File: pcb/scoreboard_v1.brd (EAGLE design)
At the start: 150 x 90 mm, 28 parts, among them U1 ESP-12F, U2 AP2111H

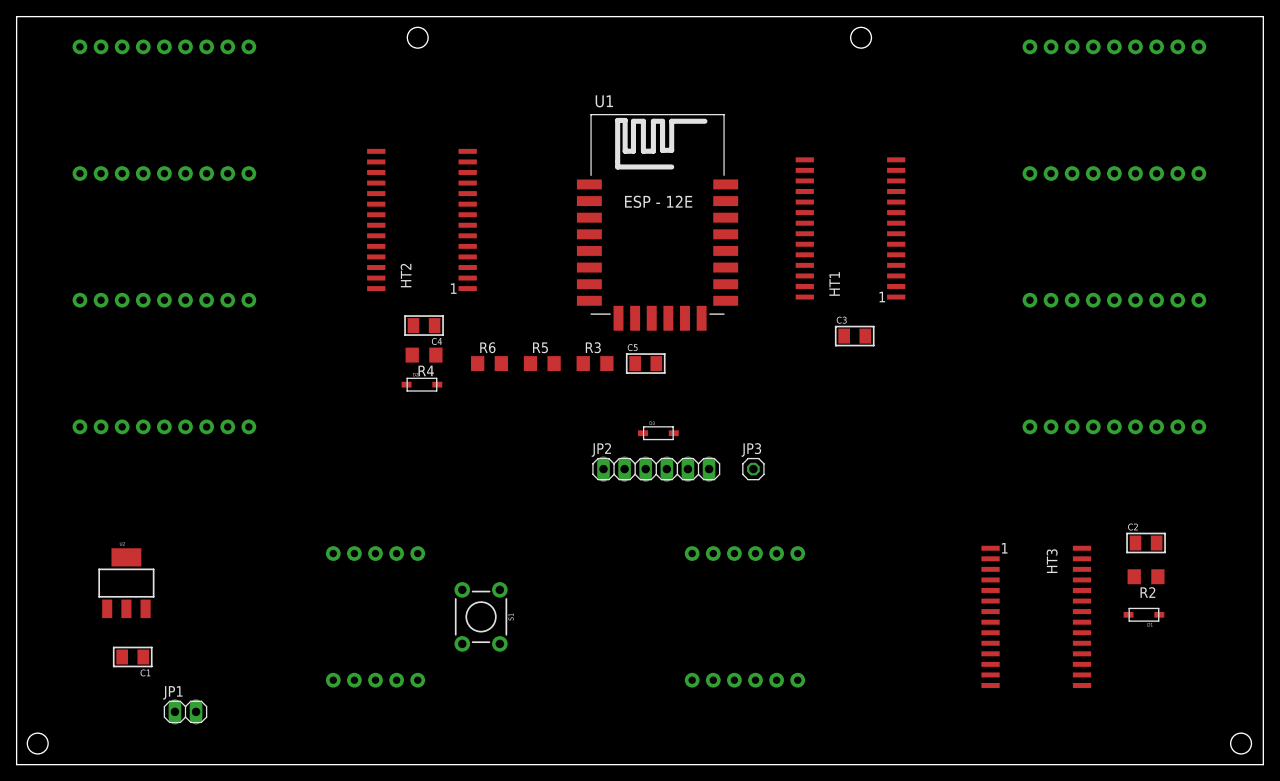
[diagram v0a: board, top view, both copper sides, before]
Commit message: PCB update for SMD version
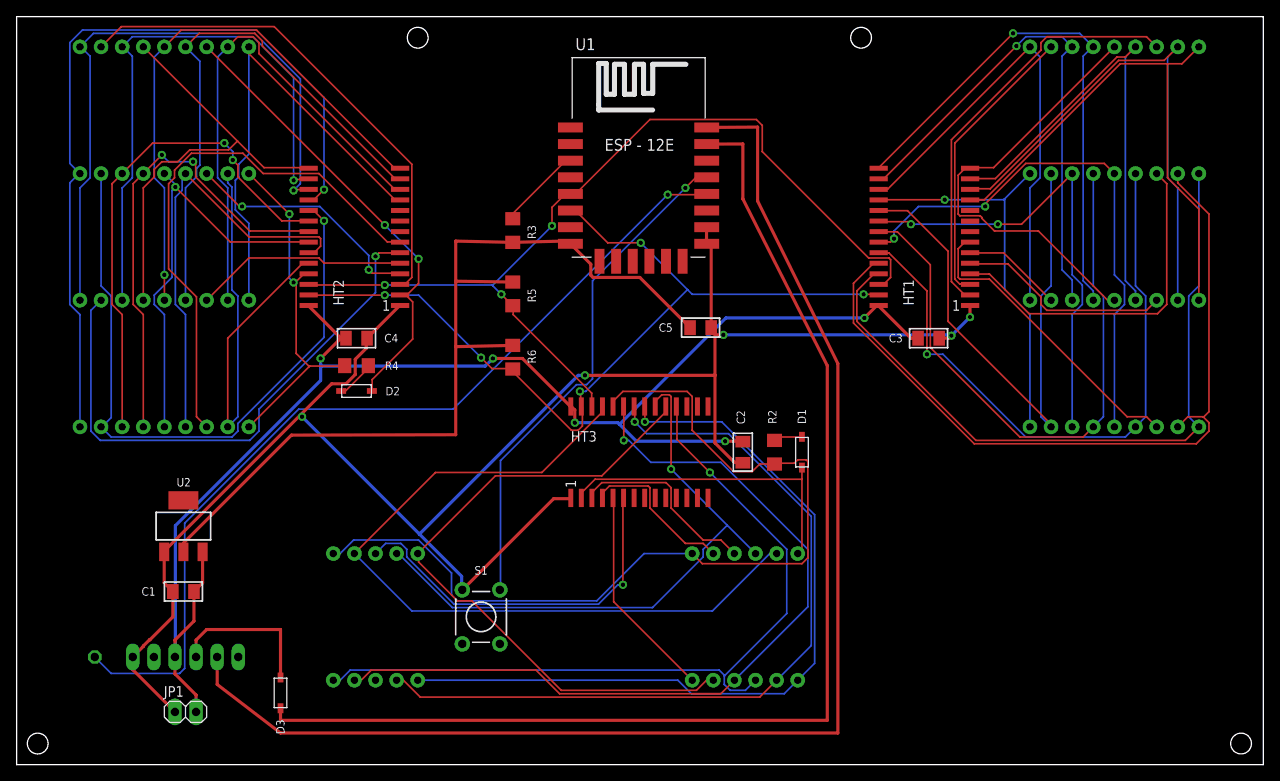
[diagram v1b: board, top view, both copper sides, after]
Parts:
- moved JP3 82.4 mm to (9.40, 13.0), flipped to the bottom
- moved JP2 61.0 mm to (20.3, 13.0), flipped to the bottom
- moved D3 55.2 mm to (31.8, 8.64), turned to 270 degrees
- moved HT3 51.7 mm to (74.9, 37.6), turned to 0 degrees
- moved C2 49.7 mm to (87.4, 37.6), turned to 90 degrees
- moved R2 47.1 mm to (91.2, 37.6), turned to 270 degrees
- moved D1 45.6 mm to (94.5, 37.6), turned to 270 degrees
- moved R3 18.8 mm to (59.7, 64.3), turned to 90 degrees
- moved C1 9.96 mm to (20.1, 20.8)
- moved U2 9.70 mm to (20.1, 28.7)
- moved R5 9.11 mm to (59.7, 56.6), turned to 90 degrees
- moved HT1 8.95 mm to (109.2, 63.5)
- moved C3 8.89 mm to (109.7, 51.3), turned to 180 degrees
- moved HT2 8.38 mm to (40.6, 63.5)
- moved C4 8.27 mm to (40.9, 51.3)
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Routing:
- net GND: track 0.00 -> 223.0 mm, vias 0 -> 5
- net +5V: track 0.00 -> 174.2 mm, vias 0 -> 5
- net TX: track 0.00 -> 161.2 mm
- net RX: track 0.00 -> 143.4 mm
- net SCL: track 0.00 -> 111.9 mm, vias 0 -> 3
- net 3.3V: track 0.00 -> 109.4 mm
- net HT3_A1: track 0.00 -> 108.7 mm
- net GPIO0: track 0.00 -> 108.6 mm, vias 0 -> 1
- net SDA: track 0.00 -> 103.7 mm, vias 0 -> 5
- net HT3_A2: track 0.00 -> 99.2 mm, vias 0 -> 1
- net HT3_A3: track 0.00 -> 96.7 mm, vias 0 -> 1
- net HT2_A7: track 0.00 -> 95.8 mm, vias 0 -> 1
- net HT1_A1: track 0.00 -> 94.9 mm
- net HT3_A4: track 0.00 -> 94.7 mm, vias 0 -> 1
- net HT3_A7: track 0.00 -> 94.5 mm, vias 0 -> 1
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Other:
- board text added: "GAME7LABS"
- board text added: "July 2018"
- board text added: "Rev B"
- board text added: "SCOREBOARD"
